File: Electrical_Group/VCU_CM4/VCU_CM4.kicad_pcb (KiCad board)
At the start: 4 copper layers, 100 x 90 mm, 452 parts, among them J1 RPI_UPS, J10 MSD-4-A, J2 VCU_UPS, J24 USB_C_stm32, J4 MIPI_DSI_22P, J5 MIPI_CAM_22P, J7 MSD-4-A, J8 Conn_01x30_Socket, J9 Conn_02x15_Odd_Even, Q1 AO3400A, Q2 MMBT3904, Q3 2N7002, Q4 AO3401A, SW1 RPI_CPU_RST, SW2 RESET, SW3 BOOT0, SW4 RESET, SW5 RESET, SW6 RPI_PWR, U1 LM66100DCK, U10 MCP2518FD, U11 REF3133AIDBZR, U12 STM32H743ZITx, U13 TPS5430DDA, U14 TCAN1042VDRQ1, U15 USB2514B_Bi, U17 TCAN1042VDRQ1, U19 TCAN1042VDRQ1, U2 TLV75733PDRV, U20 MCP7940N-xSN, U3 TPS5430DDA, U4 TCAN1042VDRQ1, U5 STM32F103CBT6, U6 TLV75733PDRV, U7 TLV75733PDRV, U8 TLV75733PDRV, U9 MCP2518FD, Y1 8MHz X50328MSB2GI, Y2 40Mhz XTM32040000DT00351001, Y3 40Mhz XTM32040000DT00351001, Y4 40Mhz XTM32040000DT00351001, Y5 32.768kHz Q13FC13500004, Y6 24Mhz X322524MOB4SI, Y7 32.768kHz Q13FC13500004

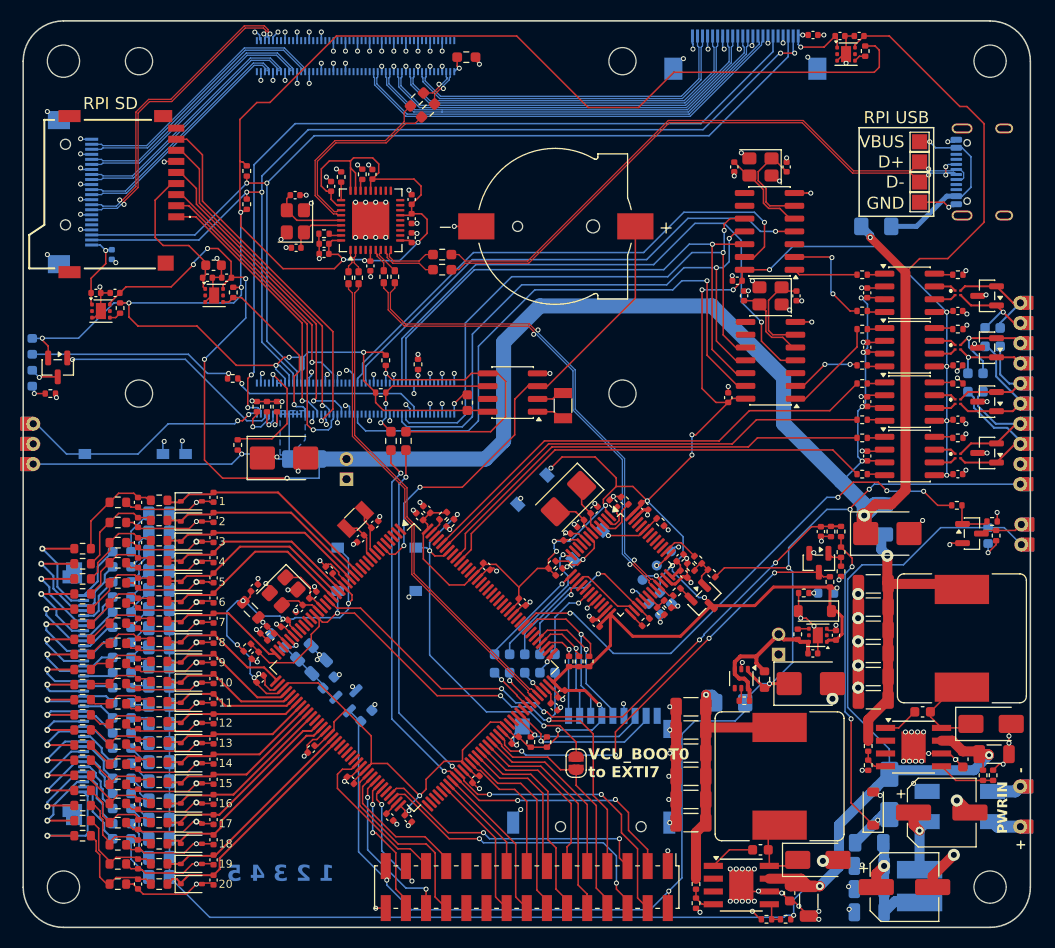
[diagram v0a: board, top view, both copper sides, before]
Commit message: vcu_cm4 minor pcb adjustment
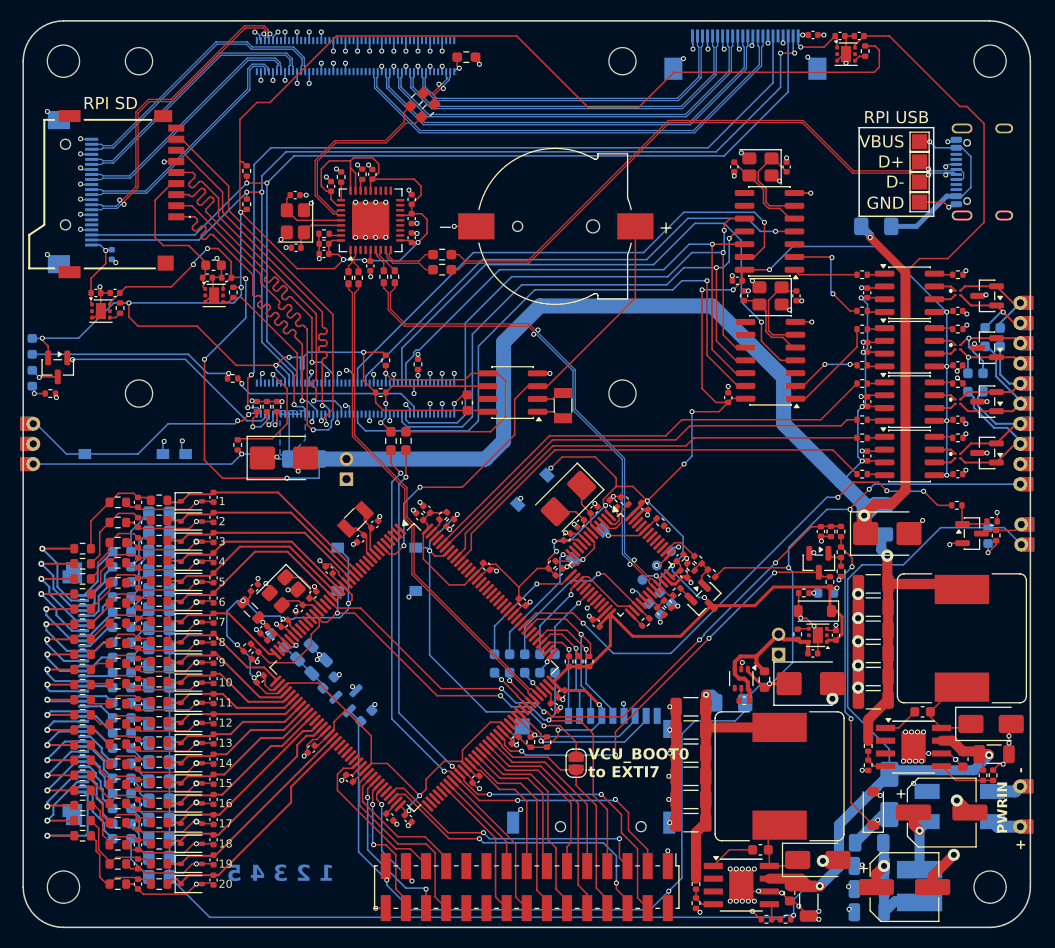
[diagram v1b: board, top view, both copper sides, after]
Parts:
- moved C96 0.22 mm to (231.4, 145.2)
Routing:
- net /computer/SD.CMD: track 26.0 -> 35.6 mm
- net /computer/SD.D2: track 26.8 -> 35.6 mm
- net /computer/SD.D3: track 31.9 -> 35.6 mm
- net /computer/SD.CK: track 32.5 -> 35.7 mm
- net /computer/SD.D0: track 32.9 -> 35.8 mm
- net /computer/compute module/CAM1.D3_P: track 44.9 -> 47.7 mm
- net /computer/compute module/CAM1.D3_N: track 44.2 -> 46.9 mm
- net /computer/compute module/CAM1.D2_P: track 42.4 -> 44.5 mm
- net /computer/compute module/CAM1.D2_N: track 41.7 -> 43.8 mm
- net /computer/SCL0: track 100.3 -> 102.4 mm
- net /computer/SDA0: track 101.1 -> 103.1 mm
- net /computer/CAM_GPIO0: track 83.9 -> 85.7 mm
- net /stlink/USART2_RX: track 11.0 -> 12.5 mm
- net /computer/compute module/CAM1.C_N: track 39.2 -> 40.6 mm
- net /computer/compute module/CAM1.C_P: track 40.0 -> 41.3 mm
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
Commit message: [VCU_CM4] V1.1
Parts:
- added C132: 100n, Capacitor_SMD:C_0402_1005Metric, F.Cu at (242.7, 118.5)
- added F26: 0.5A, Fuse:Fuse_1206_3216Metric, B.Cu at (217.1, 158.0)
- added R170: 2k2, Resistor_SMD:R_0402_1005Metric, F.Cu at (258.8, 146.3)
- added R171: 2k2, Resistor_SMD:R_0402_1005Metric, F.Cu at (258.2, 149.2)
- added R172: 2k2, Resistor_SMD:R_0402_1005Metric, F.Cu at (257.2, 149.2)
- added R173: 2k2, Resistor_SMD:R_0402_1005Metric, F.Cu at (257.6, 146.3)
- added R174: 0R, Resistor_SMD:R_0603_1608Metric_Pad0.98x0.95mm_HandSolder, B.Cu at (243.8, 133.8)
- added R175: 0R, Resistor_SMD:R_0603_1608Metric_Pad0.98x0.95mm_HandSolder, B.Cu at (242.3, 133.8)
- added R176: 0R, Resistor_SMD:R_0603_1608Metric_Pad0.98x0.95mm_HandSolder, B.Cu at (240.8, 133.8)
- F2: value 0.5A -> 1A
- J8: value Conn_01x30_Socket -> current_loops
- J9: value Conn_02x15_Odd_Even -> to_Dash_Screen
- U2, U6, U7, U8: value TLV75733PDRV -> TLV75733; footprint Package_SON:WSON-6-1EP_2x2mm_P0.65mm_EP1x1.6mm -> Package_TO_SOT_SMD:SOT-23-5
- Y4: value 40Mhz XTM32040000DT00351001 -> 8Mhz
- moved C48 7.45 mm to (213.6, 98.0), turned to -90 degrees
- moved Q4 5.80 mm to (202.5, 98.6), turned to 180 degrees
- moved R48 5.56 mm to (200.9, 101.5)
- moved C43 5.50 mm to (217.4, 100.7), turned to 0 degrees
- moved D15 5.28 mm to (199.9, 100.2)
- moved D16 5.20 mm to (199.9, 97.1)
- moved U8 4.29 mm to (211.0, 98.6)
- moved C44 4.20 mm to (282.2, 75.7), turned to 0 degrees
- moved R54 3.98 mm to (220.9, 100.8), turned to 0 degrees
- moved R55 3.09 mm to (285.3, 74.5), turned to 90 degrees
- moved C7 2.75 mm to (275.9, 130.5), turned to -90 degrees
- moved R56 2.70 mm to (209.4, 101.1), turned to 90 degrees
- moved C8 2.12 mm to (279.4, 128.9), turned to 180 degrees
- moved U7 2.11 mm to (282.8, 73.1), turned to 90 degrees
- moved D3 1.88 mm to (275.9, 127.8)
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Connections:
- net /vcu mcu/EXTI8 renamed /24V_lowTrig
- F10 pad 1: +24V -> Net-(F10-Pad1)
- F11 pad 1: +24V -> Net-(F10-Pad1)
- F12 pad 1: +24V -> Net-(F10-Pad1)
- F13 pad 1: +24V -> Net-(F10-Pad1)
- F14 pad 1: +24V -> Net-(F10-Pad1)
- F15 pad 1: +24V -> Net-(F10-Pad1)
- F16 pad 1: +24V -> Net-(F10-Pad1)
- F17 pad 1: +24V -> Net-(F10-Pad1)
- F18 pad 1: +24V -> Net-(F10-Pad1)
- F19 pad 1: +24V -> Net-(F10-Pad1)
- F20 pad 1: +24V -> Net-(F10-Pad1)
- F21 pad 1: +24V -> Net-(F10-Pad1)
- F22 pad 1: +24V -> Net-(F10-Pad1)
- F23 pad 1: +24V -> Net-(F10-Pad1)
- F24 pad 1: +24V -> Net-(F10-Pad1)
- F5 pad 1: +24V -> Net-(F10-Pad1)
- F6 pad 1: +24V -> Net-(F10-Pad1)
- F7 pad 1: +24V -> Net-(F10-Pad1)
- F8 pad 1: +24V -> Net-(F10-Pad1)
- F9 pad 1: +24V -> Net-(F10-Pad1)
- J9 pad 19: unconnected-(J9-Pin_19-Pad19) -> /vcu mcu/SPI2_CS
- J9 pad 20: unconnected-(J9-Pin_20-Pad20) -> /vcu mcu/SPI2_SCK
- J9 pad 21: unconnected-(J9-Pin_21-Pad21) -> /vcu mcu/SPI2_MOSI
- J9 pad 22: unconnected-(J9-Pin_22-Pad22) -> /vcu mcu/SPI2_MISO
- U12 pad 73: unconnected-(U12-PB12-Pad73) -> /vcu mcu/SPI2_CS
- U12 pad 74: unconnected-(U12-PB13-Pad74) -> /vcu mcu/SPI2_SCK
- U12 pad 75: unconnected-(U12-PB14-Pad75) -> /vcu mcu/SPI2_MISO
- U12 pad 76: unconnected-(U12-PB15-Pad76) -> /vcu mcu/SPI2_MOSI
- U2 pad 1: +3V3 -> /power/5V_proUPS
- U2 pad 2: unconnected-(U2-NC-Pad2) -> GND
- U2 pad 3: GND -> Net-(U2-EN)
- U2 pad 4: Net-(U2-EN) -> unconnected-(U2-NC-Pad4)
- U2 pad 5: unconnected-(U2-NC-Pad5) -> +3V3
- U6 pad 1: Net-(J7-VDD) -> +5V_CM
- U6 pad 2: unconnected-(U6-NC-Pad2) -> GND
- U6 pad 3: GND -> /computer/SD_PWR_ON
- U6 pad 4: /computer/SD_PWR_ON -> unconnected-(U6-NC-Pad4)
- U6 pad 5: unconnected-(U6-NC-Pad5) -> Net-(J7-VDD)
- U7 pad 1: /computer/3V3_CAM -> +5V_CM
- U7 pad 2: unconnected-(U7-NC-Pad2) -> GND
- U7 pad 3: GND -> Net-(U7-EN)
- U7 pad 4: Net-(U7-EN) -> unconnected-(U7-NC-Pad4)
- U7 pad 5: unconnected-(U7-NC-Pad5) -> /computer/3V3_CAM
- U8 pad 1: /computer/3V3_DISP -> +5V_CM
- U8 pad 2: unconnected-(U8-NC-Pad2) -> GND
- U8 pad 3: GND -> Net-(U8-EN)
- U8 pad 4: Net-(U8-EN) -> unconnected-(U8-NC-Pad4)
- U8 pad 5: unconnected-(U8-NC-Pad5) -> /computer/3V3_DISP
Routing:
- net +24V: track 185.2 -> 142.9 mm
- net Net-(F10-Pad1): track 0.00 -> 40.0 mm
- net /computer/40P.GPIO14: track 0.00 -> 35.1 mm, vias 0 -> 2
- net /computer/40P.GPIO15: track 0.00 -> 34.7 mm, vias 0 -> 2
- net /computer/40P.GPIO25: track 0.00 -> 31.4 mm, vias 0 -> 2
- net +5V_CM: track 235.1 -> 219.7 mm, vias 11 -> 9
- net /vcu mcu/SPI2_SCK: track 0.00 -> 13.6 mm, vias 0 -> 2
- net +3V3: track 315.2 -> 328.4 mm, vias 26 -> 27
- net +3V3_CMOUT: track 233.8 -> 220.8 mm, vias 10 -> 11
- net /vcu mcu/SPI2_MISO: track 0.00 -> 12.2 mm
- net /vcu mcu/SPI2_CS: track 0.00 -> 9.64 mm, vias 0 -> 2
- net /24V_lowTrig: track 43.1 -> 51.4 mm, vias 4 -> 5
- net /vcu mcu/SPI2_MOSI: track 0.00 -> 8.20 mm
- net /vcu mcu/BOOT0: track 39.2 -> 47.1 mm
- net /stlink/VCP_MCU_UART.RX: track 3.83 -> 9.76 mm
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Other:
- board text added: "24V FUSE"
- board text added: "CM4"
- board text added: "NOTE STLINK GND and S_DIO silkscreen is marked reveresed should fix in the next version"
- board text added: "P14"
- board text added: "P15"
- board text added: "P25"
- board text added: "REF3133"
- board text added: "RPI"
- board text added: "RPI USB2.0"
- board text added: "T_RX"
- board text added: "T_TX"
- board text added: "VCU VREF SELECT"
- board text added: "VCU_CM4 V1.1 26/05/23"
- board text added: "current loop main fuse"
- board text removed: "RX"
- board text removed: "TX"
- board text removed: "VCU VREF"
- board text removed: "VCU_CM4 V1.0 26/05/22"
